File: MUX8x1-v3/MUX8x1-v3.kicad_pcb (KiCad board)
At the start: 4 copper layers, 151.1 x 73.7 mm, 38 parts, among them J1 Conn_01x09_Male, J10 Conn_01x03_Male, J11 Conn_01x09_Male, J12 Conn_01x09_Male, J14 Conn_01x09_Male, J15 Conn_01x09_Male, J16 Conn_01x09_Male, J18 Conn_01x09_Male, J19 Conn_01x09_Male, J2 Conn_01x09_Male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

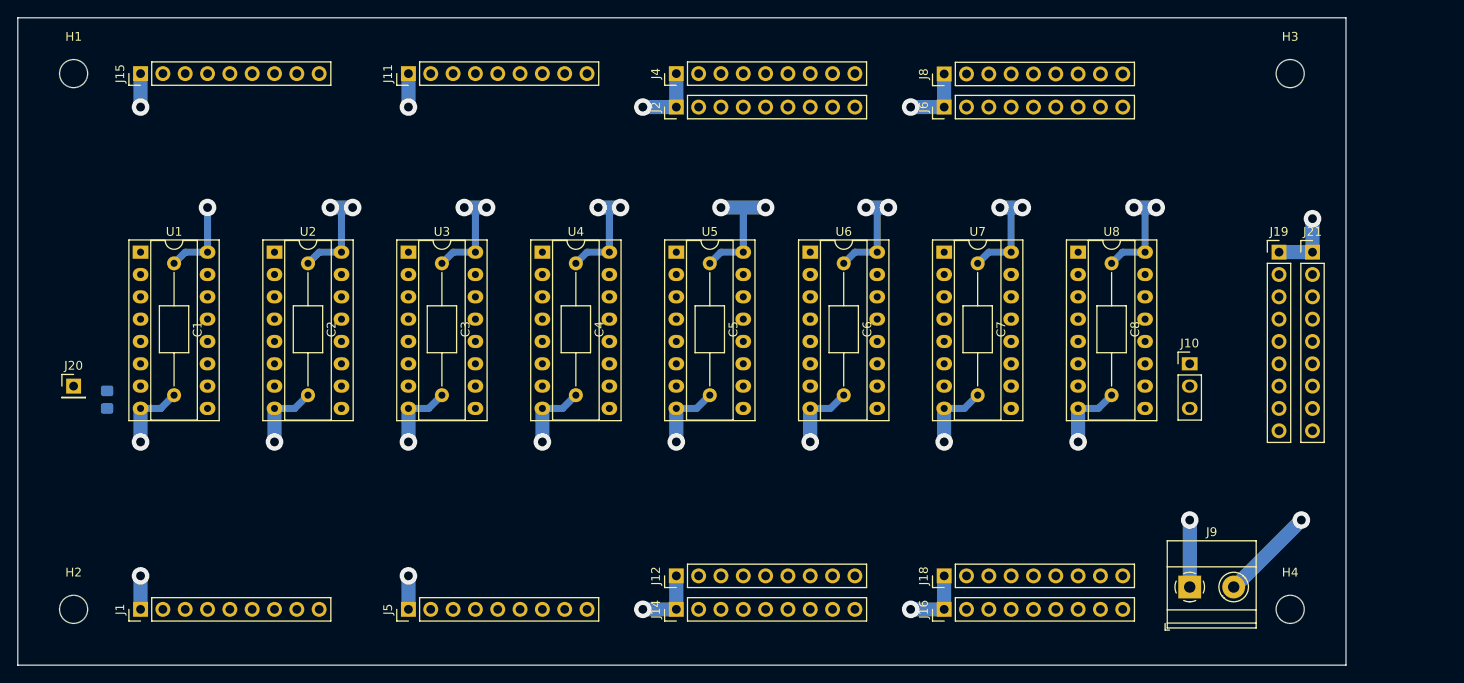
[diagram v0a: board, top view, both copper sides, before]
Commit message: MUX8x1, 4 layer, first try
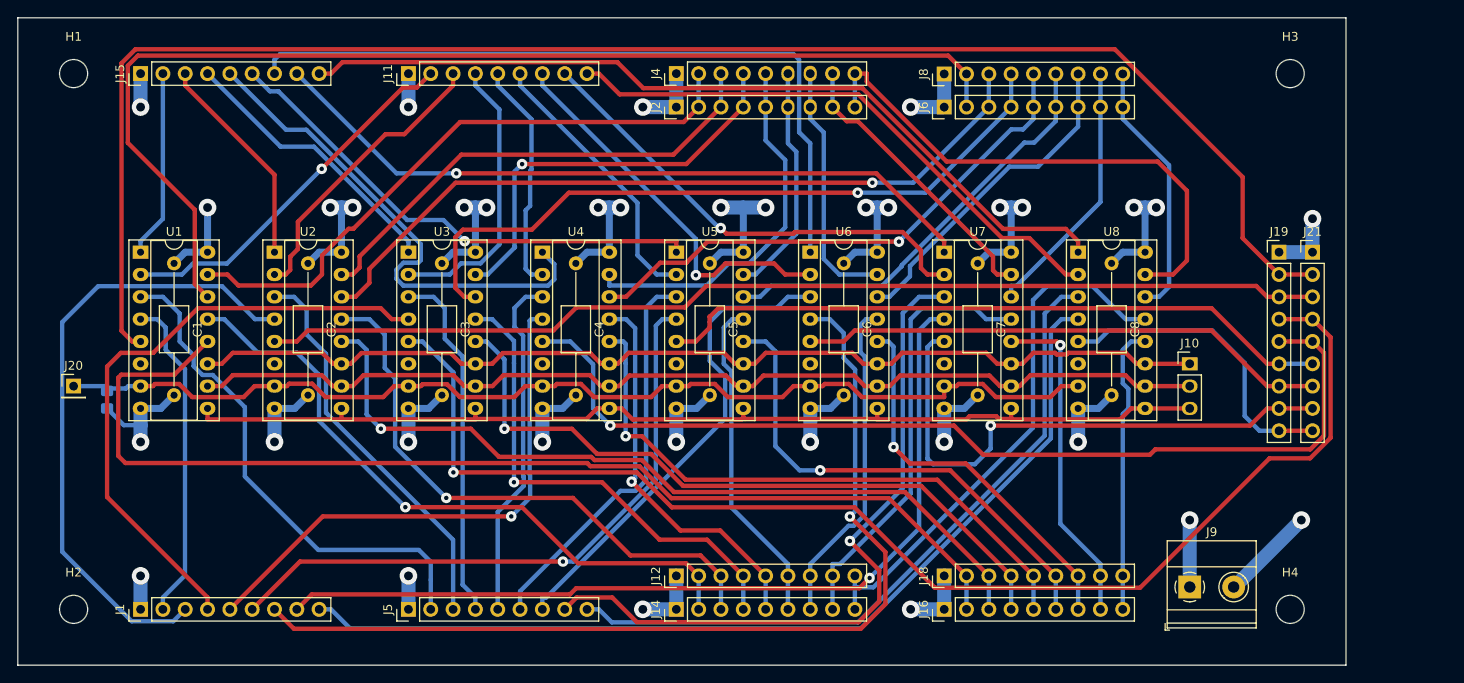
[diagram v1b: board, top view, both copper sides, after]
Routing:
- net /O0: track 0.00 -> 184.0 mm
- net /O2: track 0.00 -> 148.4 mm, vias 0 -> 1
- net /F0: track 0.00 -> 130.6 mm
- net /H0: track 0.00 -> 126.7 mm
- net /~E: track 0.00 -> 124.2 mm
- net /O1: track 0.00 -> 121.2 mm
- net /S2: track 0.00 -> 121.0 mm
- net /S0: track 0.00 -> 119.8 mm
- net /S1: track 0.00 -> 118.9 mm
- net /O3: track 0.00 -> 113.2 mm, vias 0 -> 1
- net /A5: track 0.00 -> 109.4 mm, vias 0 -> 1
- net /A7: track 0.00 -> 109.1 mm
- net /A6: track 0.00 -> 100.5 mm, vias 0 -> 1
- net /D7: track 0.00 -> 96.6 mm
- net /H1: track 0.00 -> 92.8 mm, vias 0 -> 1
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
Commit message: MUX8x1 polishing
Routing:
- net /O0: track 184.0 -> 191.7 mm
- net /F2: track 81.6 -> 88.5 mm
- net /O2: track 148.4 -> 154.4 mm
- net /C7: track 65.3 -> 70.7 mm
- net /F0: track 130.6 -> 125.7 mm
- net /C0: track 42.5 -> 47.3 mm
- net /A6: track 100.5 -> 104.9 mm
- net /A5: track 109.4 -> 113.5 mm
- net /D7: track 96.6 -> 100.7 mm
- net /O3: track 113.2 -> 117.1 mm
- net /D3: track 58.1 -> 61.4 mm
- net /A4: track 72.2 -> 75.5 mm
- net /C2: track 32.3 -> 35.1 mm
- net /B4: track 45.2 -> 47.9 mm
- net /E2: track 47.3 -> 50.0 mm
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
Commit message: MUX8:1 in work
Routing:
- net /C1: track 35.1 -> 44.9 mm
- net /A3: track 61.1 -> 69.6 mm
- net /G3: track 44.5 -> 52.1 mm
- net /G0: track 74.9 -> 82.2 mm
- net /G2: track 55.8 -> 62.1 mm
- net /A4: track 75.5 -> 80.9 mm
- net /E0: track 69.9 -> 75.3 mm
- net /H1: track 92.8 -> 98.1 mm
- net /C0: track 47.3 -> 51.9 mm
- net /D6: track 83.9 -> 88.4 mm
- net /D7: track 100.7 -> 105.0 mm
- net /B0: track 58.1 -> 62.3 mm
- net /E1: track 55.6 -> 59.7 mm
- net /F1: track 87.3 -> 91.4 mm
- net /G1: track 65.9 -> 69.9 mm
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
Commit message: Polishing MUX8:1 v3 (150x70)
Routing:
- net VCC: track 251.2 -> 236.0 mm, vias 16 -> 10
- net /A6: track 106.9 -> 116.5 mm
- net /A7: track 109.1 -> 113.6 mm
- net /B7: track 80.0 -> 84.4 mm
- net /A5: track 114.6 -> 118.6 mm
- net /A1: track 71.4 -> 74.2 mm
- net /O6: track 63.1 -> 65.7 mm
- net /B6: track 82.8 -> 80.4 mm, vias 1 -> 0
- net /G6: track 49.7 -> 51.6 mm
- net /G5: track 37.7 -> 39.6 mm
- net /E6: track 36.7 -> 34.8 mm
- net /H3: track 69.3 -> 70.9 mm
- net /H5: track 44.4 -> 45.9 mm
- net /G7: track 61.1 -> 62.4 mm
- net /F3: track 61.8 -> 63.1 mm
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
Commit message: MUX8:1 remake
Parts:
- removed J19: Conn_01x09_Male, Connector_PinHeader_2.54mm:PinHeader_1x09_P2.54mm_Vertical
- added C9: 0.1uF, Capacitor_THT:C_Axial_L5.1mm_D3.1mm_P15.00mm_Horizontal, F.Cu at (168.9, 64.8)
- added D1: LED, LED_SMD:LED_0805_2012Metric_Pad1.15x1.40mm_HandSolder, F.Cu at (157.5, 89.9)
- added D2: LED, LED_SMD:LED_0805_2012Metric_Pad1.15x1.40mm_HandSolder, F.Cu at (154.9, 89.9)
- added D3: LED, LED_SMD:LED_0805_2012Metric_Pad1.15x1.40mm_HandSolder, F.Cu at (152.4, 89.9)
- added J3: Conn_01x09_Male, Connector_PinHeader_2.54mm:PinHeader_1x09_P2.54mm_Vertical, F.Cu at (180.3, 63.5)
- added J7: Conn_01x01_Male, Connector_PinHeader_2.54mm:PinHeader_1x01_P2.54mm_Vertical, F.Cu at (180.3, 58.4)
- added R2: 10k, Resistor_SMD:R_0805_2012Metric_Pad1.20x1.40mm_HandSolder, B.Cu at (169.2, 55.9)
- added R3: 10k, Resistor_SMD:R_0805_2012Metric_Pad1.20x1.40mm_HandSolder, F.Cu at (179.1, 55.2)
- added R4: 1k, Resistor_SMD:R_0805_2012Metric_Pad1.20x1.40mm_HandSolder, F.Cu at (157.5, 85.4)
- added R5: 1k, Resistor_SMD:R_0805_2012Metric_Pad1.20x1.40mm_HandSolder, F.Cu at (154.9, 85.4)
- added R6: 1k, Resistor_SMD:R_0805_2012Metric_Pad1.20x1.40mm_HandSolder, F.Cu at (152.4, 85.4)
- added U9: 74HC245, Package_DIP:DIP-20_W7.62mm_Socket, F.Cu at (165.1, 58.4)
- moved J21 13.7 mm to (184.2, 63.5)
- moved J10 10.2 mm to (157.5, 81.3), turned to 270 degrees
- moved H3 2.54 mm to (171.4, 38.1)
- moved H4 2.54 mm to (171.4, 99.1)
- moved J9 1.27 mm to (157.5, 97.8)
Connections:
- J21 pad 1: GND -> /BUS0
- J21 pad 2: /O0 -> /BUS1
- J21 pad 3: /O1 -> /BUS2
- J21 pad 4: /O2 -> /BUS3
- J21 pad 5: /O3 -> /BUS4
- J21 pad 6: /O4 -> /BUS5
- J21 pad 7: /O5 -> /BUS6
- J21 pad 8: /O6 -> /BUS7
- J21 pad 9: /O7 -> GND
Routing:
- net VCC: track 236.0 -> 48.8 mm, vias 10 -> 0
- net GND: track 137.7 -> 83.9 mm, vias 18 -> 1
- net /O3: track 118.2 -> 103.2 mm
- net /~OE: track 0.00 -> 12.7 mm
- net /S0: track 119.6 -> 132.1 mm
- net /BUS7: track 0.00 -> 11.4 mm
- net /BUS6: track 0.00 -> 11.4 mm
- net /BUS5: track 0.00 -> 11.4 mm
- net /BUS4: track 0.00 -> 11.4 mm
- net /BUS3: track 0.00 -> 11.4 mm
- net /BUS2: track 0.00 -> 11.4 mm
- net /BUS1: track 0.00 -> 11.4 mm
- net /BUS0: track 0.00 -> 11.4 mm
- net /O6: track 65.7 -> 55.7 mm
- net /S1: track 120.6 -> 128.3 mm
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- added copper zone on In1.Cu, net VCC
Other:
- board size 151.1 x 73.7 mm -> 162.6 x 73.7 mm
- board text added: "0"
- board text added: "7"
- board text added: "A"
- board text added: "B"
- board text added: "C"
- board text added: "D"
- board text added: "E"
- board text added: "F"
- board text added: "G"
- board text added: "Gnd"
- board text added: "H"
- board text added: "S0"
- board text added: "S1"
- board text added: "S2"
- board text added: "Vcc"
- board text added: "Zero"
- board text added: "~OE"
